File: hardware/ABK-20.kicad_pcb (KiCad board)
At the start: 2 copper layers, 90 x 90 mm, 77 parts, among them J1 CONN_01X04, J2 CONN_01X04, J3 CONN_02X03, J4 Con_3-5V, J5 USB_C_6P, J6 Sync_Jumper, SW1 SW_SPST, SW2 SW_Push, SW3 SW_SPDT_MSM, SW4 SW_Push, U1 ATTINY85-20SU, U2 PAM8002, U3 7805

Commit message: feat(footprint): update slide pot to Bourns PTL30 (30mm travel, +-20mm column pitch)
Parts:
- RV1: footprint 8Bitmixtape_reworked:Potentiometer_Bourns_PTL20_Single_Slide_LED -> 8Bitmixtape_reworked:Potentiometer_Bourns_PTL30_Single_Slide_LED
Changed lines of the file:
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@@
 		)
 	)
-	(footprint "8Bitmixtape_reworked:Potentiometer_Bourns_PTL20_Single_Slide_LED"
+	(footprint "8Bitmixtape_reworked:Potentiometer_Bourns_PTL30_Single_Slide_LED"
 		(layer "B.Cu")
 		(at 110 188)
-		(descr "Bourns PTL20 Series Slide Potentiometer with integrated LED, 20mm travel, https://www.bourns.com/docs/product-datasheets/ptl.pdf")
-		(tags "Bourns PTL20 slide potentiometer fader LED illuminated 20mm")
+		(descr "Bourns PTL30 Series Slide Potentiometer with integrated LED, 30mm travel, https://www.bourns.com/docs/product-datasheets/ptl.pdf")
+		(tags "Bourns PTL30 slide potentiometer fader LED illuminated 30mm")
 		(property "Reference" "RV1"
 			(at 0 -5.8 0)
@@
 		(attr through_hole)
 		(fp_line
-			(start -17.62 -4.62)
-			(end 17.62 -4.62)
-			(stroke
-				(width 0.12)
-				(type solid)
-			)
-			(layer "F.SilkS")
-		)
-		(fp_line
-			(start -17.62 4.62)
-			(end -17.62 -4.62)
-			(stroke
-				(width 0.12)
-				(type solid)
-			)
-			(layer "F.SilkS")
-		)
-		(fp_line
-			(start 17.62 -4.62)
-			(end 17.62 4.62)
-			(stroke
-				(width 0.12)
-				(type solid)
-			)
-			(layer "F.SilkS")
-		)
-		(fp_line
-			(start 17.62 4.62)
-			(end -17.62 4.62)
+			(start -22.62 -4.62)
+			(end 22.62 -4.62)
+			(stroke
+				(width 0.12)
+				(type solid)
+			)
+			(layer "F.SilkS")
+		)
+		(fp_line
+			(start -22.62 4.62)
+			(end -22.62 -4.62)
+			(stroke
+				(width 0.12)
+				(type solid)
+			)
+			(layer "F.SilkS")
+		)
+		(fp_line
+			(start 22.62 -4.62)
+			(end 22.62 4.62)
+			(stroke
+				(width 0.12)
+				(type solid)
+			)
+			(layer "F.SilkS")
+		)
+		(fp_line
+			(start 22.62 4.62)
+			(end -22.62 4.62)
 			(stroke
 				(width 0.12)
@@
 		)
 		(fp_rect
-			(start -17.75 -4.75)
-			(end 17.75 4.75)
+			(start -22.75 -4.75)
+			(end 22.75 4.75)
 			(stroke
 				(width 0.05)
@@
 		)
 		(fp_line
-			(start -17.5 -4.5)
-			(end 17.5 -4.5)
-			(stroke
-				(width 0.1)
-				(type solid)
-			)
-			(layer "F.Fab")
-		)
-		(fp_line
-			(start -17.5 4.5)
-			(end -17.5 -4.5)
-			(stroke
-				(width 0.1)
-				(type solid)
-			)
-			(layer "F.Fab")
-		)
-		(fp_line
-			(start -10 -0.8)
-			(end 10 -0.8)
-			(stroke
-				(width 0.1)
-				(type solid)
-			)
-			(layer "F.Fab")
-		)
-		(fp_line
-			(start -10 0.8)
-			(end -10 -0.8)
-			(stroke
-				(width 0.1)
-				(type solid)
-			)
-			(layer "F.Fab")
-		)
-		(fp_line
-			(start 10 -0.8)
-			(end 10 0.8)
-			(stroke
-				(width 0.1)
-				(type solid)
-			)
-			(layer "F.Fab")
-		)
-		(fp_line
-			(start 10 0.8)
-			(end -10 0.8)
-			(stroke
-				(width 0.1)
-				(type solid)
-			)
-			(layer "F.Fab")
-		)
-		(fp_line
-			(start 17.5 -4.5)
-			(end 17.5 4.5)
-			(stroke
-				(width 0.1)
-				(type solid)
-			)
-			(layer "F.Fab")
-		)
-		(fp_line
-			(start 17.5 4.5)
-			(end -17.5 4.5)
+			(start -22.5 -4.5)
+			(end 22.5 -4.5)
+			(stroke
+				(width 0.1)
+				(type solid)
+			)
+			(layer "F.Fab")
+		)
+		(fp_line
+			(start -22.5 4.5)
+			(end -22.5 -4.5)
+			(stroke
+				(width 0.1)
+				(type solid)
+			)
+			(layer "F.Fab")
+		)
+		(fp_line
+			(start -18.5 -0.8)
+			(end 18.5 -0.8)
+			(stroke
+				(width 0.1)
+				(type solid)
+			)
+			(layer "F.Fab")
+		)
+		(fp_line
+			(start -18.5 0.8)
+			(end -18.5 -0.8)
+			(stroke
+				(width 0.1)
+				(type solid)
+			)
+			(layer "F.Fab")
+		)
+		(fp_line
+			(start 18.5 -0.8)
+			(end 18.5 0.8)
+			(stroke
+				(width 0.1)
+				(type solid)
+			)
+			(layer "F.Fab")
+		)
+		(fp_line
+			(start 18.5 0.8)
+			(end -18.5 0.8)
+			(stroke
+				(width 0.1)
+				(type solid)
+			)
+			(layer "F.Fab")
+		)
+		(fp_line
+			(start 22.5 -4.5)
+			(end 22.5 4.5)
+			(stroke
+				(width 0.1)
+				(type solid)
+			)
+			(layer "F.Fab")
+		)
+		(fp_line
+			(start 22.5 4.5)
+			(end -22.5 4.5)
 			(stroke
 				(width 0.1)
@@
 		)
 		(fp_circle
-			(center -15.5 0)
-			(end -14.5 0)
+			(center -20.5 0)
+			(end -19.5 0)
 			(stroke
 				(width 0.1)
@@
 		)
 		(fp_circle
-			(center 15.5 0)
-			(end 16.5 0)
+			(center 20.5 0)
+			(end 21.5 0)
 			(stroke
 				(width 0.1)
@@
 		)
 		(fp_text user "-E"
-			(at -12.8 3.75 0)
+			(at -17.8 3.75 0)
 			(layer "F.SilkS")
 			(effects
@@
 		)
 		(fp_text user "1"
-			(at -13 -1.25 0)
+			(at -18 -1.25 0)
 			(layer "F.SilkS")
 			(effects
@@
 		)
 		(fp_text user "+B"
-			(at 12.8 3.75 0)
+			(at 17.8 3.75 0)
 			(layer "F.SilkS")
 			(effects
@@
 		)
 		(fp_text user "2"
-			(at -13 -3.75 0)
+			(at -18 -3.75 0)
 			(layer "F.SilkS")
 			(effects
@@
 		)
 		(fp_text user "3"
-			(at 13 -1.25 0)
+			(at 18 -1.25 0)
 			(layer "F.SilkS")
 			(effects
@@
 		)
 		(pad "1" thru_hole rect
-			(at -15 -1.25)
+			(at -20 -1.25)
 			(size 1.8 1.8)
 			(drill 1.2)
@@
 		)
 		(pad "2" thru_hole circle
-			(at -15 -3.75)
+			(at -20 -3.75)
 			(size 1.8 1.8)
 			(drill 1.2)
@@
 		)
 		(pad "3" thru_hole circle
-			(at 15 -1.25)
+			(at 20 -1.25)
 			(size 1.8 1.8)
 			(drill 1.2)
@@
 		)
 		(pad "4" thru_hole circle
-			(at -15 3.75)
+			(at -20 3.75)
 			(size 1.8 1.8)
 			(drill 1.2)
@@
 		)
 		(pad "5" thru_hole circle
-			(at 15 3.75)
+			(at 20 3.75)
 			(size 1.8 1.8)
 			(drill 1.2)
@@
 		)
 		(pad "L" thru_hole circle
-			(at -15 1.25)
-			(size 1.8 1.8)
-			(drill 1.2)
+			(at -20 1.25)
+			(size 1.8 1.8)
+			(drill 1.2)

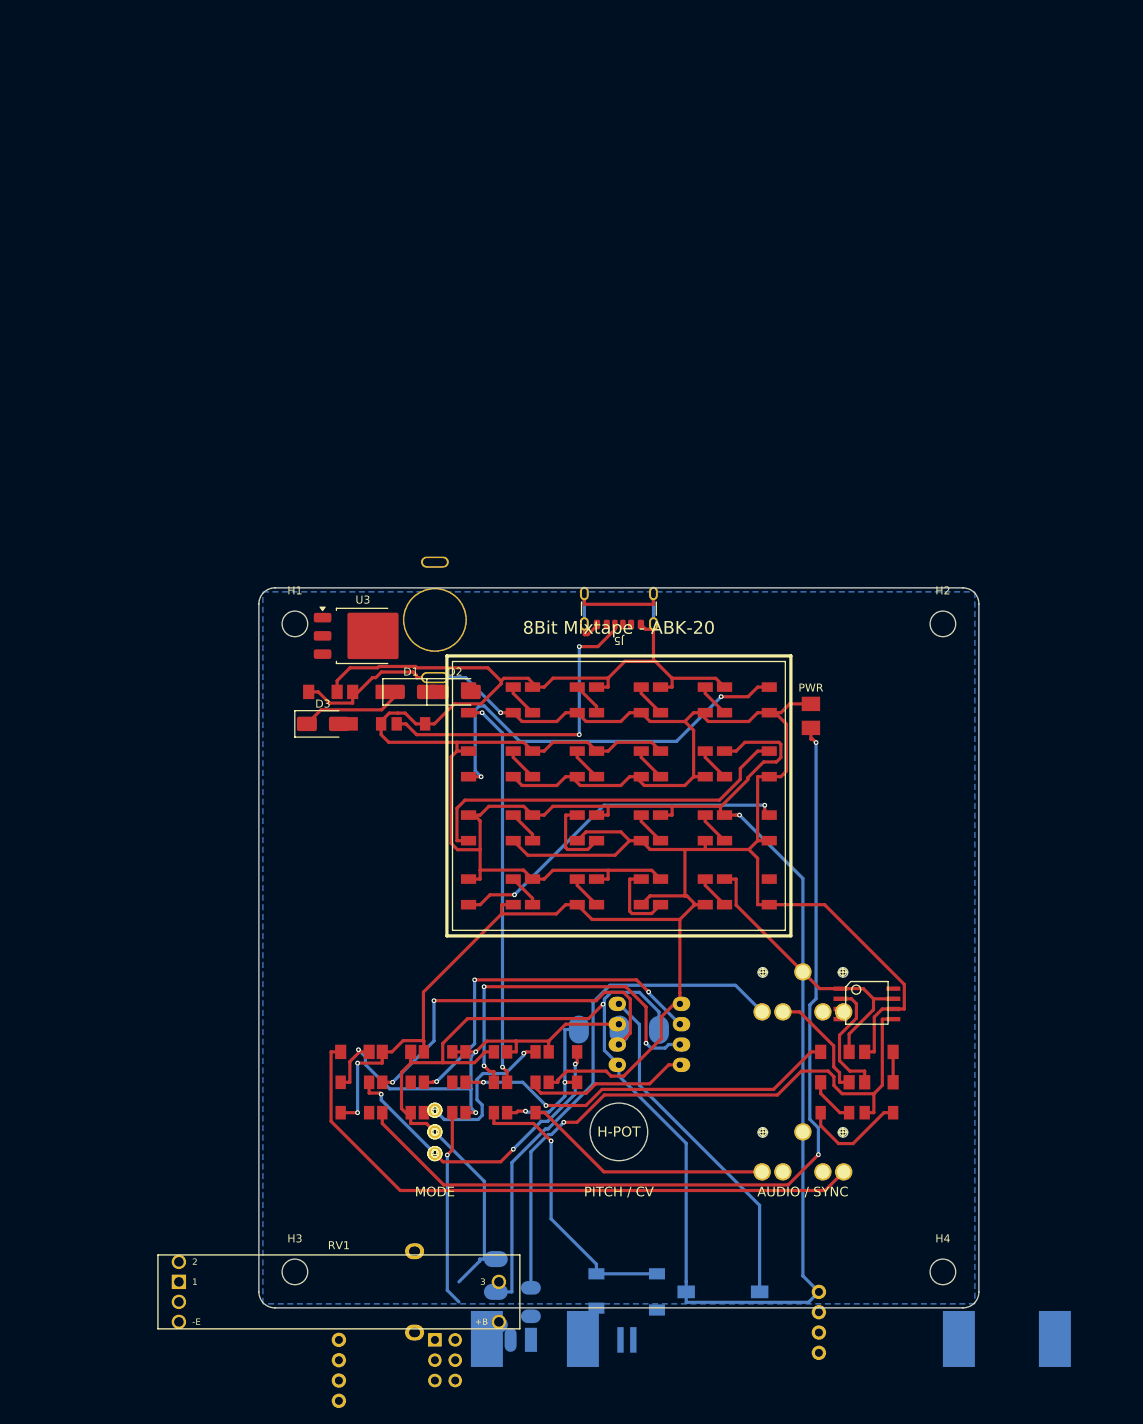
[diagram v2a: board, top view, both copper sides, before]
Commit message: fix(pcb): update all 67 component 3D models to valid paths in current board layout
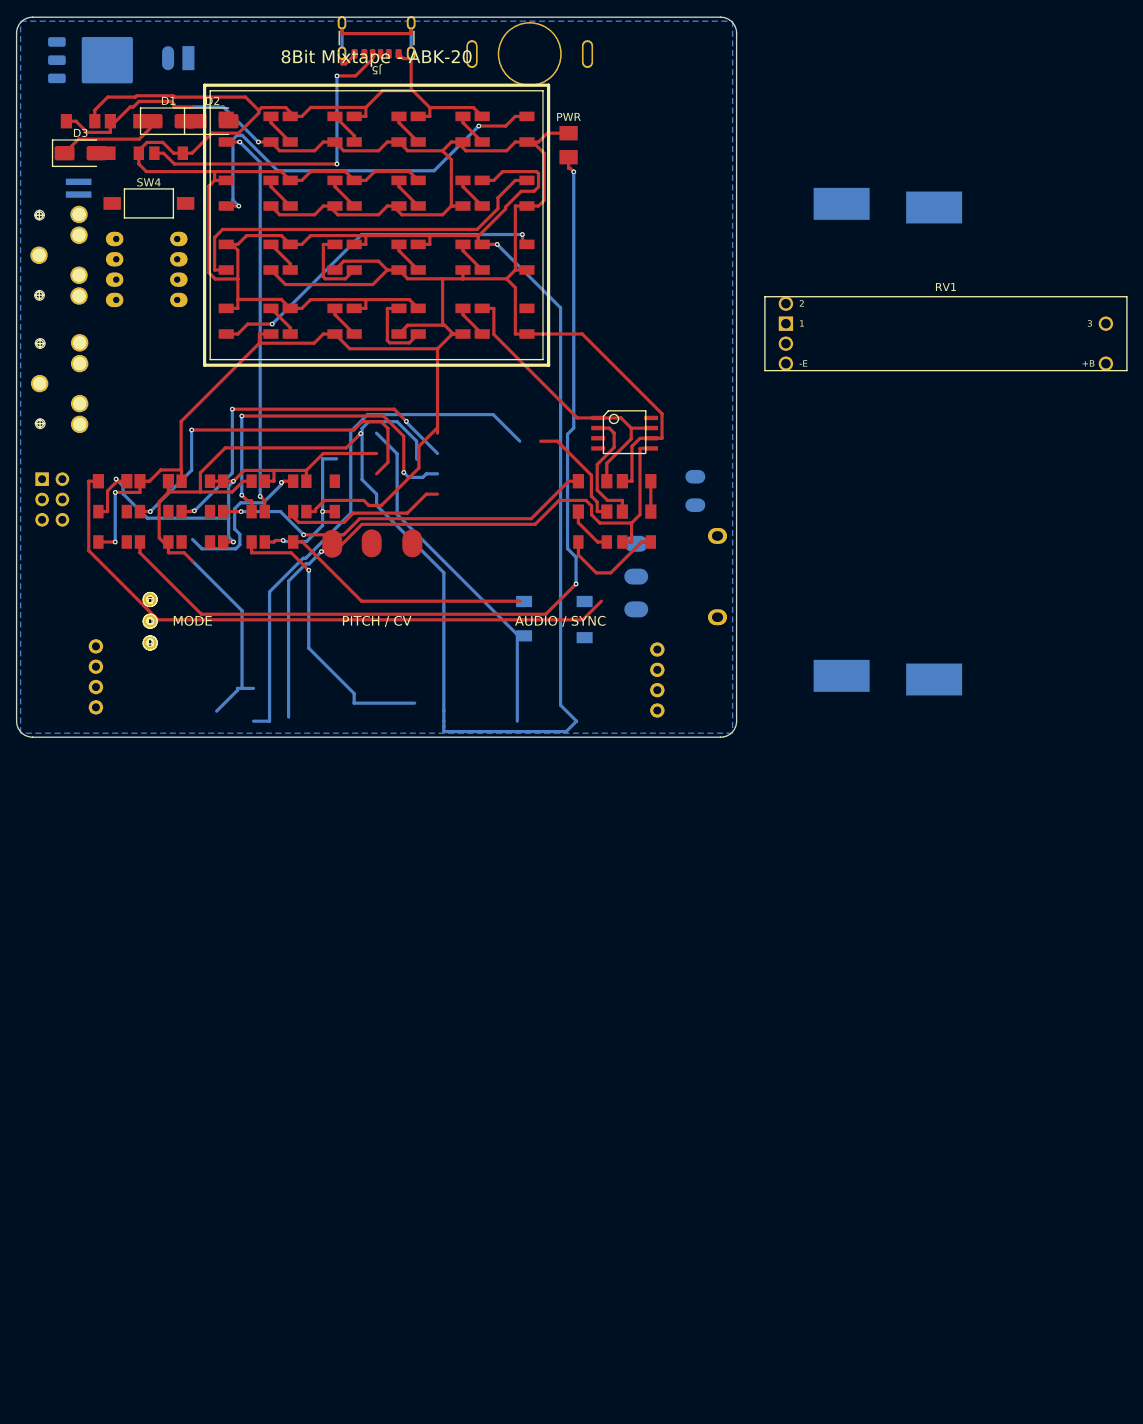
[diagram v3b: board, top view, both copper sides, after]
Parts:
- removed H-POT: , 
- removed H1, H2, H3, H4: MountingHole_3.2mm_M3, MountingHole_3.2mm_M3
- POT2-CV1, RV1, SW4, U3: moved to F.Cu
- moved J4 165.8 mm to (91.2, 33.8)
- moved J6 159.4 mm to (77.5, 50.0), turned to -90 degrees
- moved SW4 153.8 mm to (86.3, 51.9), turned to 0 degrees
- moved RV1 141.8 mm to (185.9, 68.2)
- moved Jack1 133.6 mm to (72.6, 74.5), turned to 0 degrees
- moved Jack2 130.9 mm to (72.5, 58.4), turned to 0 degrees
- moved J3 118.3 mm to (72.9, 86.4)
- moved U1 114.4 mm to (82.2, 56.4)
- moved BT1 113.5 mm to (173.0, 81.5), turned to -90 degrees
- moved BT2 113.0 mm to (184.3, 82.0), turned to 90 degrees
- moved Speaker1 103.4 mm to (154.6, 86.6)
- moved POT3-Vol1 95.2 mm to (154.8, 98.6), turned to 0 degrees
- moved J2 84.7 mm to (79.6, 114.9), turned to 0 degrees
- moved SW2 84.5 mm to (137.0, 104.0)
- moved J1 82.8 mm to (149.8, 107.7)
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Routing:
- net GND: track 510.4 -> 553.7 mm
- net Net-(U1-PB5(~{RESET}/dW/ADC0/PCINT5)): track 43.3 -> 0.00 mm
- net But-R: track 40.0 -> 0.00 mm, vias 3 -> 0
- net Net-(RV1B-A): track 24.5 -> 0.00 mm, vias 1 -> 0
